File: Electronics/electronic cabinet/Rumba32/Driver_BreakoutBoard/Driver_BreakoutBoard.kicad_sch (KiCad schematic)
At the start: 14 parts, among them IC1 SN74ACT32PWR, J1 Conn_01x08, J2 Conn_01x08, J3 Conn_01x02, J4 0393570002, J5 Conn_01x02, Q1 Q_NPN_CEB

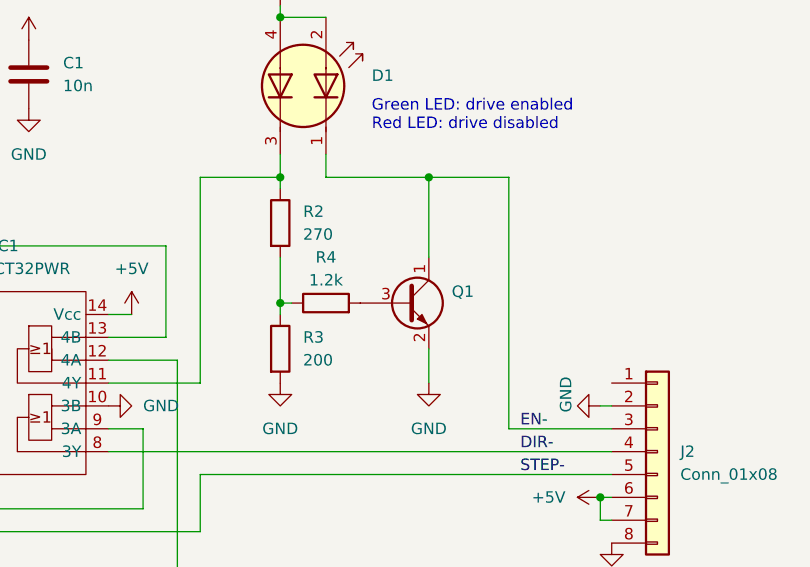
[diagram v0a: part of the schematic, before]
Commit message: Updated with new PCB Layout.
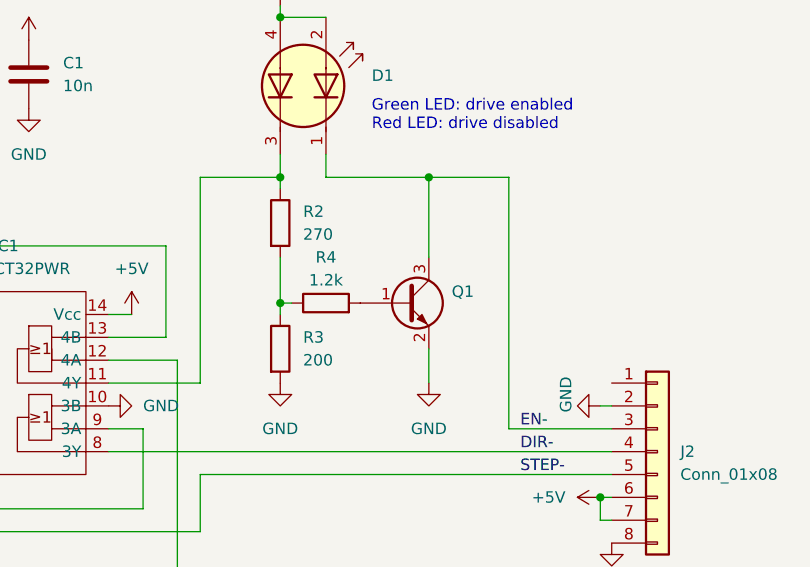
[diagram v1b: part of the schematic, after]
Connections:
- net EN-: now also Q1.3 (C); no longer Q1.1 (C)
- net at R4.2: now also Q1.1 (B); no longer Q1.3 (B)
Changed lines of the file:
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@@
       (effects (font (size 1.27 1.27)) (justify left))
     )
-    (property "Value" "Q_NPN_CEB" (id 1) (at 133.35 92.7099 0)
+    (property "Value" "Q_NPN_CEB" (id 1) (at 140.97 100.33 0)
       (effects (font (size 1.27 1.27)) (justify left) hide)
     )
-    (property "Footprint" "Package_TO_SOT_SMD:SOT-23_Handsoldering" (id 2) (at 133.35 88.9 0)
+    (property "Footprint" "Package_TO_SOT_SMD:SOT-23_Handsoldering" (id 2) (at 154.94 83.82 0)
       (effects (font (size 1.27 1.27)) hide)
     )
-    (property "Datasheet" "https://assets.nexperia.com/documents/data-sheet/MMBT3904.pdf" (id 3) (at 128.27 91.44 0)
+    (property "Datasheet" "https://assets.nexperia.com/documents/data-sheet/MMBT3904.pdf" (id 3) (at 132.08 104.14 0)
       (effects (font (size 1.27 1.27)) hide)
     )
